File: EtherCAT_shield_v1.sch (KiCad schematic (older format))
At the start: 18 parts, among them J1 RJ45-PULSETRANS, J2 RJ45-PULSETRANS, P1 CONN_02X10, P2 CONN_02X19, P3 CONN_02X19, U1 LAN9252

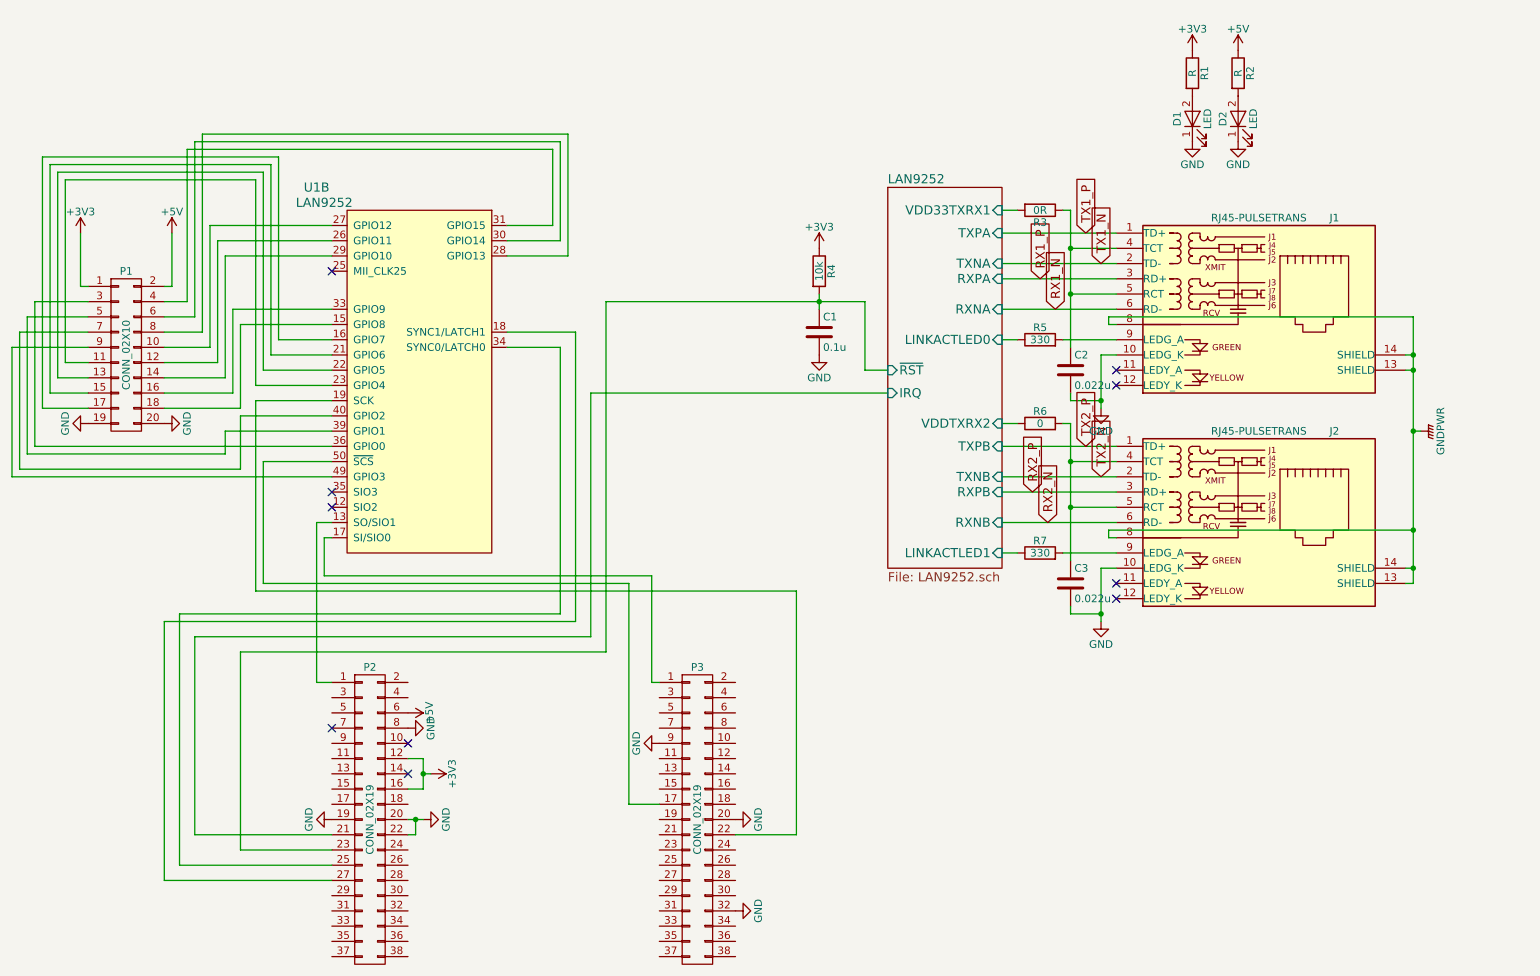
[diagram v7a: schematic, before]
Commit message: LED変更，再アノテーション
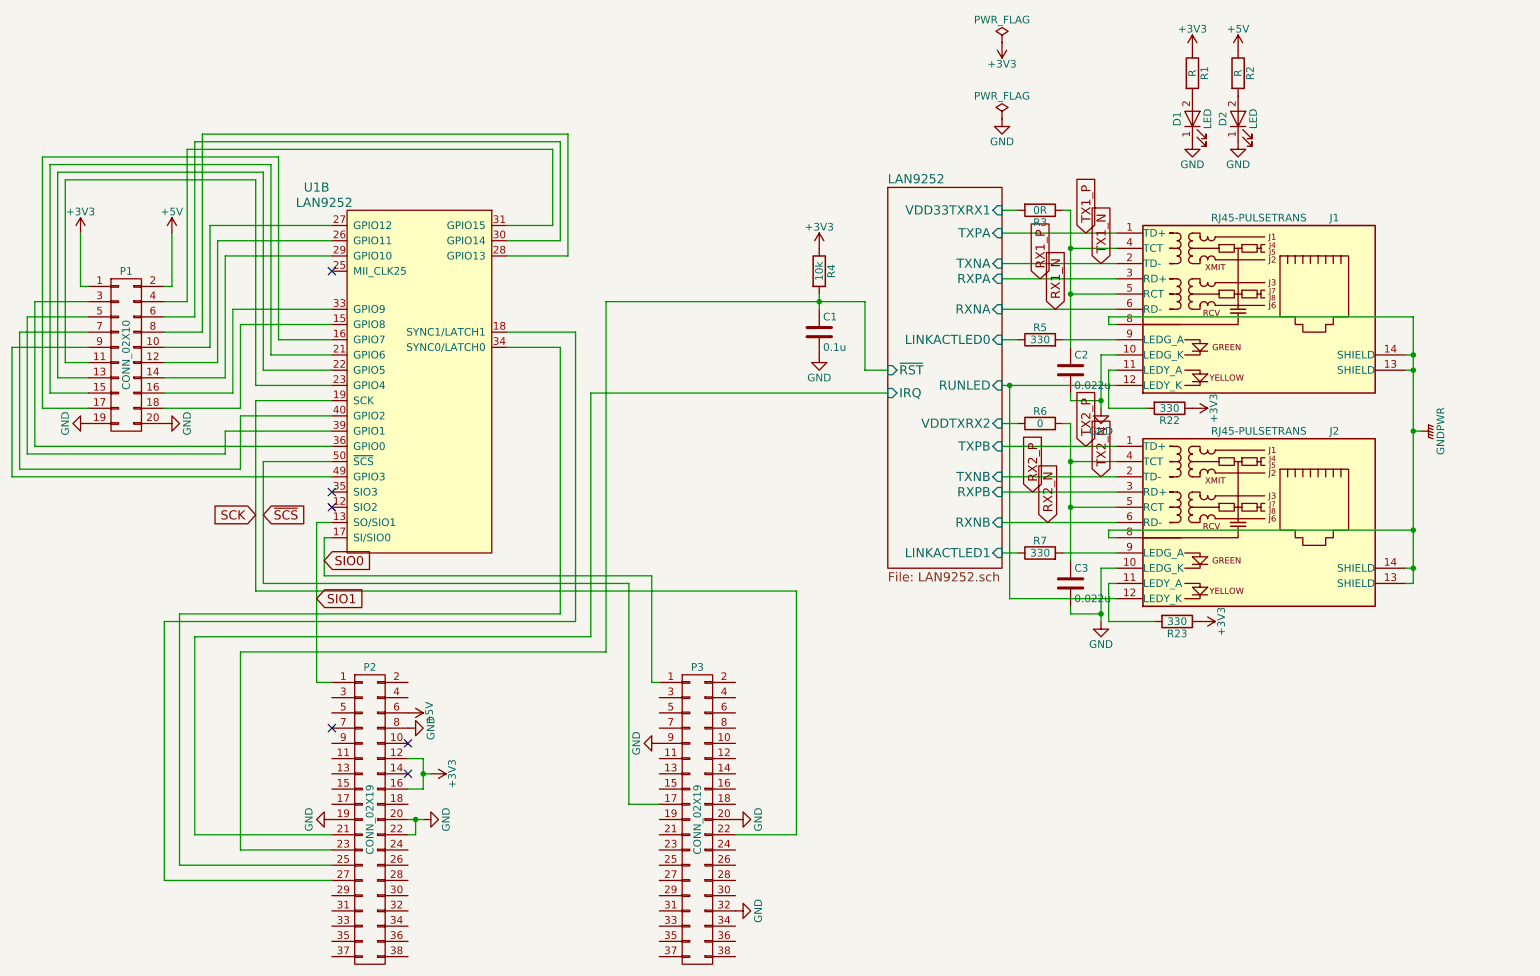
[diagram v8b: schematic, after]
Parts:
- added R22, R23: 330, Resistors_SMD:R_0603, symbol R
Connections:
- net +3V3: now also R22.1, R23.1
- net at J1.11 (LEDY_A): now also R22.2
- net LAN9252/RUNLED: now reaches J1.12 (LEDY_K)
- net LAN9252/RUNLED: now also J2.12 (LEDY_K)
- net at J2.11 (LEDY_A): now also R23.2
- net SIO1: now reaches P2.1 (P1), U1.13 (SO/SIO1)
- net SIO0: now reaches P3.1 (P1), U1.17 (SI/SIO0)
- net SCK: now reaches P3.22 (P22), U1.19 (SCK)
- net ~SCS: now reaches P3.17 (P17), U1.50 (~SCS)
- no-connect marks 10 -> 6
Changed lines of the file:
@@
 F14 "~RST" I L 6950 3150 60
 F15 "IRQ" I L 6950 3300 60
+F16 "RUNLED" I R 7700 3250 60
 $EndSheet
 NoConn ~ 3300 2500
@@
 	0    1    1    0
 $EndComp
-NoConn ~ 8450 3150
-NoConn ~ 8450 3250
-NoConn ~ 8450 4550
-NoConn ~ 8450 4650
 $Comp
 L C C2
@@
 	2200 6500 3300 6500
 $Comp
-L +5V #PWR?
+L +5V #PWR021
 U 1 1 58DD1482
 P 3800 5400
-F 0 "#PWR?" H 3800 5250 50  0001 C CNN
+F 0 "#PWR021" H 3800 5250 50  0001 C CNN
 F 1 "+5V" H 3800 5540 50  0000 C CNN
 F 2 "" H 3800 5400 50  0001 C CNN
@@
 	0    1    1    0
 $EndComp
+Text GLabel 3250 4400 2    60   Input ~ 0
+SIO0
+Text GLabel 3200 4650 2    60   Input ~ 0
+SIO1
+Text GLabel 2850 4100 2    60   Input ~ 0
+~SCS
+Text GLabel 2800 4100 0    60   Input ~ 0
+SCK
+$Comp
+L PWR_FLAG #FLG022
+U 1 1 58DDF543
+P 7700 1000
+F 0 "#FLG022" H 7700 1075 50  0001 C CNN
+F 1 "PWR_FLAG" H 7700 1150 50  0000 C CNN
+F 2 "" H 7700 1000 50  0001 C CNN
+F 3 "" H 7700 1000 50  0001 C CNN
+	1    7700 1000
+	1    0    0    -1
+$EndComp
+$Comp
+L PWR_FLAG #FLG023
+U 1 1 58DDF5CF
+P 7700 1500
+F 0 "#FLG023" H 7700 1575 50  0001 C CNN
+F 1 "PWR_FLAG" H 7700 1650 50  0000 C CNN
+F 2 "" H 7700 1500 50  0001 C CNN
+F 3 "" H 7700 1500 50  0001 C CNN
+	1    7700 1500
+	1    0    0    -1
+$EndComp
+$Comp
+L +3V3 #PWR024
+U 1 1 58DDFCFB
+P 7700 1000
+F 0 "#PWR024" H 7700 850 50  0001 C CNN
+F 1 "+3V3" H 7700 1140 50  0000 C CNN
+F 2 "" H 7700 1000 50  0000 C CNN
+F 3 "" H 7700 1000 50  0000 C CNN
+	1    7700 1000
+	-1   0    0    1
+$EndComp
+$Comp
+L GND #PWR025
+U 1 1 58DE0004
+P 7700 1500
+F 0 "#PWR025" H 7700 1250 50  0001 C CNN
+F 1 "GND" H 7700 1350 50  0000 C CNN
+F 2 "" H 7700 1500 50  0000 C CNN
+F 3 "" H 7700 1500 50  0000 C CNN
+	1    7700 1500
+	1    0    0    -1
+$EndComp
+Wire Wire Line
+	8450 3250 7700 3250
+Wire Wire Line
+	8450 4650 7750 4650
+Wire Wire Line
+	7750 4650 7750 3250
+Connection ~ 7750 3250
+Wire Wire Line
+	8450 3150 8400 3150
+Wire Wire Line
+	8400 3150 8400 3400
+Wire Wire Line
+	8400 3400 8650 3400
+$Comp
+L R R22
+U 1 1 58DEBDC1
+P 8800 3400
+F 0 "R22" V 8880 3400 50  0000 C CNN
+F 1 "330" V 8800 3400 50  0000 C CNN
+F 2 "Resistors_SMD:R_0603" V 8730 3400 50  0001 C CNN
+F 3 "" H 8800 3400 50  0001 C CNN
+	1    8800 3400
+	0    1    1    0
+$EndComp
+Wire Wire Line
+	8450 4550 8400 4550
+Wire Wire Line
+	8400 4550 8400 4800
+Wire Wire Line
+	8400 4800 8700 4800
+$Comp
+L R R23
+U 1 1 58DECF32
+P 8850 4800
+F 0 "R23" V 8930 4800 50  0000 C CNN
+F 1 "330" V 8850 4800 50  0000 C CNN
+F 2 "Resistors_SMD:R_0603" V 8780 4800 50  0001 C CNN
+F 3 "" H 8850 4800 50  0001 C CNN
+	1    8850 4800
+	0    1    1    0
+$EndComp
+$Comp
+L +3V3 #PWR026
+U 1 1 58DEDAC2
+P 8950 3400
+F 0 "#PWR026" H 8950 3250 50  0001 C CNN
+F 1 "+3V3" H 8950 3540 50  0000 C CNN
+F 2 "" H 8950 3400 50  0000 C CNN
+F 3 "" H 8950 3400 50  0000 C CNN
+	1    8950 3400
+	0    1    1    0
+$EndComp
+$Comp
+L +3V3 #PWR027
+U 1 1 58DEE6D0
+P 9000 4800
+F 0 "#PWR027" H 9000 4650 50  0001 C CNN
+F 1 "+3V3" H 9000 4940 50  0000 C CNN
+F 2 "" H 9000 4800 50  0000 C CNN
+F 3 "" H 9000 4800 50  0000 C CNN
+	1    9000 4800
+	0    1    1    0
+$EndComp
